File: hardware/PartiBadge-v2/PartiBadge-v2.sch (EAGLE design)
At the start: 29 parts, among them IC2 TSMP58000, J1 I2C, J2 Supply, U1 1042

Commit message: mode switch to power and other cosmetic changes
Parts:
- removed R8: 100, rcl:R-US_M0805
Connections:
- removed net N$2: PHOTON.D2, S5.P
- removed net N$3: R8.1, S5.S
- new net NC: S5.S
- new net ON: IC1.IN, S5.O
- net +3V3: no longer R8.2
- net BATT: now also S5.P; no longer IC1.IN
- net CENT: now also PHOTON.D2; no longer PHOTON.D3
- net DOWN: now also PHOTON.D5; no longer PHOTON.D6
- net GND: no longer S5.O
- net LEFT: now also PHOTON.D4; no longer PHOTON.D5
- net RIGHT: now also PHOTON.D3; no longer PHOTON.D4
- net UP: now also PHOTON.D6; no longer PHOTON.D7
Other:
- moved on the sheet: S5, U1
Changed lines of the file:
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@@
 <?xml version="1.0" encoding="utf-8"?>
 <!DOCTYPE eagle SYSTEM "eagle.dtd">
-<eagle version="9.0.1">
+<eagle version="9.1.0">
 <drawing>
 <settings>
@@
 <part name="JOYSTICK" library="SparkFun-Switches" library_urn="urn:adsk.eagle:library:535" deviceset="JOYSTICK_MINI" device="" package3d_urn="urn:adsk.eagle:package:40157/1"/>
 <part name="GND6" library="supply1" library_urn="urn:adsk.eagle:library:371" deviceset="GND" device=""/>
-<part name="+3V6" library="supply1" library_urn="urn:adsk.eagle:library:371" deviceset="+3V3" device=""/>
 <part name="PARTIFRAME" library="SparkFun-Aesthetics" library_urn="urn:adsk.eagle:library:507" deviceset="FRAME-LETTER" device="NO_PACKAGE" package3d_urn="urn:adsk.eagle:package:37104/1">
 <attribute name="DESIGNER" value="Brandon Satrom"/>
 </part>
-<part name="R8" library="rcl" library_urn="urn:adsk.eagle:library:334" deviceset="R-US_" device="M0805" package3d_urn="urn:adsk.eagle:package:23556/1" value="100"/>
 <part name="PHOTON" library="Particle-Devices" deviceset="PHOTON" device="_WITH_HEADERS"/>
 <part name="U$5" library="tft_1.8_1.44_oled_0.96" deviceset="OLED_0.96_I2C" device=""/>
@@
 <part name="+3V5" library="supply1" library_urn="urn:adsk.eagle:library:371" deviceset="+3V3" device=""/>
 <part name="GND10" library="supply1" library_urn="urn:adsk.eagle:library:371" deviceset="GND" device=""/>
-<part name="GND11" library="supply1" library_urn="urn:adsk.eagle:library:371" deviceset="GND" device=""/>
 <part name="IC1" library="v-reg" library_urn="urn:adsk.eagle:library:409" deviceset="78XXS" device="" package3d_urn="urn:adsk.eagle:package:30342/1"/>
 <part name="GND9" library="supply1" library_urn="urn:adsk.eagle:library:371" deviceset="GND" device=""/>
@@
 <attribute name="VALUE" x="-35.549109375" y="71.114559375" size="1.679990625" layer="96"/>
 </instance>
-<instance part="S5" gate="1" x="68.58" y="40.64"/>
+<instance part="S5" gate="1" x="35.56" y="116.84" rot="MR0"/>
 <instance part="R5" gate="G$1" x="104.14" y="66.04" rot="R90"/>
 <instance part="R6" gate="G$1" x="124.46" y="66.04" rot="R90"/>
@@
 <instance part="JOYSTICK" gate="G$1" x="104.14" y="116.84"/>
 <instance part="GND6" gate="1" x="81.28" y="114.3" rot="R270"/>
-<instance part="+3V6" gate="G$1" x="86.36" y="58.42"/>
 <instance part="PARTIFRAME" gate="G$1" x="-60.96" y="-40.64" smashed="yes">
 <attribute name="DESIGNER" x="-60.96" y="-40.64" size="1.778" layer="96" display="off"/>
@@
 </instance>
 <instance part="PARTIFRAME" gate="V" x="86.36" y="-40.64"/>
-<instance part="R8" gate="G$1" x="86.36" y="48.26" rot="R90"/>
 <instance part="PHOTON" gate="G$1" x="35.56" y="58.42"/>
 <instance part="U$5" gate="G$1" x="-15.24" y="111.76" rot="R270"/>
@@
 <instance part="C2" gate="G$1" x="63.5" y="-20.32"/>
 <instance part="+3V5" gate="G$1" x="81.28" y="-5.08"/>
-<instance part="GND10" gate="1" x="60.96" y="106.68"/>
-<instance part="GND11" gate="1" x="78.74" y="43.18" rot="R90"/>
+<instance part="GND10" gate="1" x="73.66" y="106.68"/>
 <instance part="IC1" gate="1" x="20.32" y="124.46" rot="R180"/>
 <instance part="GND9" gate="1" x="35.56" y="127"/>
@@
 <instance part="VDD2" gate="G$1" x="7.62" y="129.54"/>
 <instance part="IC2" gate="G$1" x="53.34" y="-10.16" rot="R180"/>
-<instance part="U1" gate="G$1" x="55.88" y="116.84" rot="R180"/>
+<instance part="U1" gate="G$1" x="68.58" y="116.84" rot="R180"/>
 </instances>
 <busses>
@@
 </segment>
 <segment>
-<pinref part="S5" gate="1" pin="O"/>
-<pinref part="GND11" gate="1" pin="GND"/>
-<wire x1="76.2" y1="43.18" x2="73.66" y2="43.18" width="0.1524" layer="91"/>
-</segment>
-<segment>
 <pinref part="IC1" gate="1" pin="GND"/>
 <pinref part="GND9" gate="1" pin="GND"/>
@@
 <pinref part="U1" gate="G$1" pin="NEG"/>
 <pinref part="GND10" gate="1" pin="GND"/>
-<wire x1="55.88" y1="116.84" x2="60.96" y2="116.84" width="0.1524" layer="91"/>
-<wire x1="60.96" y1="116.84" x2="60.96" y2="109.22" width="0.1524" layer="91"/>
+<wire x1="68.58" y1="116.84" x2="73.66" y2="116.84" width="0.1524" layer="91"/>
+<wire x1="73.66" y1="116.84" x2="73.66" y2="109.22" width="0.1524" layer="91"/>
 </segment>
 </net>
@@
 <pinref part="+3V4" gate="G$1" pin="+3V3"/>
 <wire x1="127" y1="12.7" x2="127" y2="17.78" width="0.1524" layer="91"/>
-</segment>
-<segment>
-<pinref part="R8" gate="G$1" pin="2"/>
-<pinref part="+3V6" gate="G$1" pin="+3V3"/>
-<wire x1="86.36" y1="53.34" x2="86.36" y2="55.88" width="0.1524" layer="91"/>
 </segment>
 <segment>
@@
 <segment>
 <pinref part="PHOTON" gate="G$1" pin="D0"/>
-<wire x1="53.34" y1="30.48" x2="58.42" y2="30.48" width="0.1524" layer="91"/>
-<label x="53.34" y="30.48" size="1.778" layer="95"/>
+<wire x1="53.34" y1="30.48" x2="66.04" y2="30.48" width="0.1524" layer="91"/>
+<label x="58.42" y="30.48" size="1.778" layer="95"/>
 </segment>
 <segment>
@@
 <segment>
 <pinref part="PHOTON" gate="G$1" pin="D1"/>
-<wire x1="53.34" y1="35.56" x2="58.42" y2="35.56" width="0.1524" layer="91"/>
-<label x="53.34" y="35.56" size="1.778" layer="95"/>
+<wire x1="53.34" y1="35.56" x2="66.04" y2="35.56" width="0.1524" layer="91"/>
+<label x="58.42" y="35.56" size="1.778" layer="95"/>
 </segment>
 <segment>
@@
 </segment>
 <segment>
-<pinref part="PHOTON" gate="G$1" pin="D7"/>
-<wire x1="53.34" y1="66.04" x2="63.5" y2="66.04" width="0.1524" layer="91"/>
-<label x="60.96" y="66.04" size="1.778" layer="95"/>
+<pinref part="PHOTON" gate="G$1" pin="D6"/>
+<wire x1="53.34" y1="60.96" x2="66.04" y2="60.96" width="0.1524" layer="91"/>
+<label x="58.42" y="60.96" size="1.778" layer="95"/>
 </segment>
 </net>
@@
 </segment>
 <segment>
-<pinref part="PHOTON" gate="G$1" pin="D6"/>
-<wire x1="53.34" y1="60.96" x2="63.5" y2="60.96" width="0.1524" layer="91"/>
-<label x="56.642" y="60.96" size="1.778" layer="95"/>
+<pinref part="PHOTON" gate="G$1" pin="D5"/>
+<wire x1="53.34" y1="55.88" x2="66.04" y2="55.88" width="0.1524" layer="91"/>
+<label x="58.42" y="55.88" size="1.778" layer="95"/>
 </segment>
 </net>
@@
 </segment>
 <segment>
-<pinref part="PHOTON" gate="G$1" pin="D5"/>
-<wire x1="53.34" y1="55.88" x2="63.5" y2="55.88" width="0.1524" layer="91"/>
-<label x="58.42" y="55.88" size="1.778" layer="95"/>
+<pinref part="PHOTON" gate="G$1" pin="D4"/>
+<wire x1="53.34" y1="50.8" x2="66.04" y2="50.8" width="0.1524" layer="91"/>
+<label x="58.674" y="51.054" size="1.778" layer="95"/>
 </segment>
 </net>
@@
 </segment>
 <segment>
-<pinref part="PHOTON" gate="G$1" pin="D4"/>
-<wire x1="53.34" y1="50.8" x2="63.5" y2="50.8" width="0.1524" layer="91"/>
-<label x="56.896" y="51.054" size="1.778" layer="95"/>
+<pinref part="PHOTON" gate="G$1" pin="D3"/>
+<wire x1="53.34" y1="45.72" x2="66.04" y2="45.72" width="0.1524" layer="91"/>
+<label x="58.42" y="45.72" size="1.778" layer="95"/>
 </segment>
 </net>
@@
 </segment>
 <segment>
-<pinref part="PHOTON" gate="G$1" pin="D3"/>
-<wire x1="53.34" y1="45.72" x2="63.5" y2="45.72" width="0.1524" layer="91"/>
-<label x="58.42" y="45.72" size="1.778" layer="95"/>
+<pinref part="PHOTON" gate="G$1" pin="D2"/>
+<wire x1="53.34" y1="40.64" x2="66.04" y2="40.64" width="0.1524" layer="91"/>
+<label x="58.42" y="40.64" size="1.778" layer="95"/>
 </segment>
 </net>
@@
 </segment>
 </net>
-<net name="N$2" class="0">
-<segment>
-<pinref part="PHOTON" gate="G$1" pin="D2"/>
-<pinref part="S5" gate="1" pin="P"/>
-<wire x1="53.34" y1="40.64" x2="66.04" y2="40.64" width="0.1524" layer="91"/>
-</segment>
-</net>
-<net name="N$3" class="0">
-<segment>
-<pinref part="S5" gate="1" pin="S"/>
-<wire x1="73.66" y1="38.1" x2="86.36" y2="38.1" width="0.1524" layer="91"/>
-<pinref part="R8" gate="G$1" pin="1"/>
-<wire x1="86.36" y1="38.1" x2="86.36" y2="43.18" width="0.1524" layer="91"/>
-</segment>
-</net>
 <net name="5V" class="0">
 <segment>
@@
 <net name="BATT" class="0">
 <segment>
+<pinref part="U1" gate="G$1" pin="POS"/>
+<pinref part="S5" gate="1" pin="P"/>
+<wire x1="43.18" y1="116.84" x2="38.1" y2="116.84" width="0.1524" layer="91"/>
+</segment>
+</net>
+<net name="ON" class="0">
+<segment>
+<pinref part="S5" gate="1" pin="O"/>
 <pinref part="IC1" gate="1" pin="IN"/>
-<pinref part="U1" gate="G$1" pin="POS"/>
-<wire x1="27.94" y1="124.46" x2="30.48" y2="124.46" width="0.1524" layer="91"/>
-<wire x1="30.48" y1="124.46" x2="30.48" y2="116.84" width="0.1524" layer="91"/>
-</segment>
-</net>
+<wire x1="30.48" y1="119.38" x2="30.48" y2="124.46" width="0.1524" layer="91"/>
+<wire x1="30.48" y1="124.46" x2="27.94" y2="124.46" width="0.1524" layer="91"/>
+<label x="30.48" y="119.38" size="1.778" layer="95" rot="R90"/>
+</segment>
+</net>
+<net name="NC" class="0">
+<segment>
+<pinref part="S5" gate="1" pin="S"/>
+<wire x1="30.48" y1="114.3" x2="25.4" y2="114.3" width="0.1524" layer="91"/>
+<label x="25.4" y="114.3" size="1.778" layer="95"/>
+</segment>
+</net>

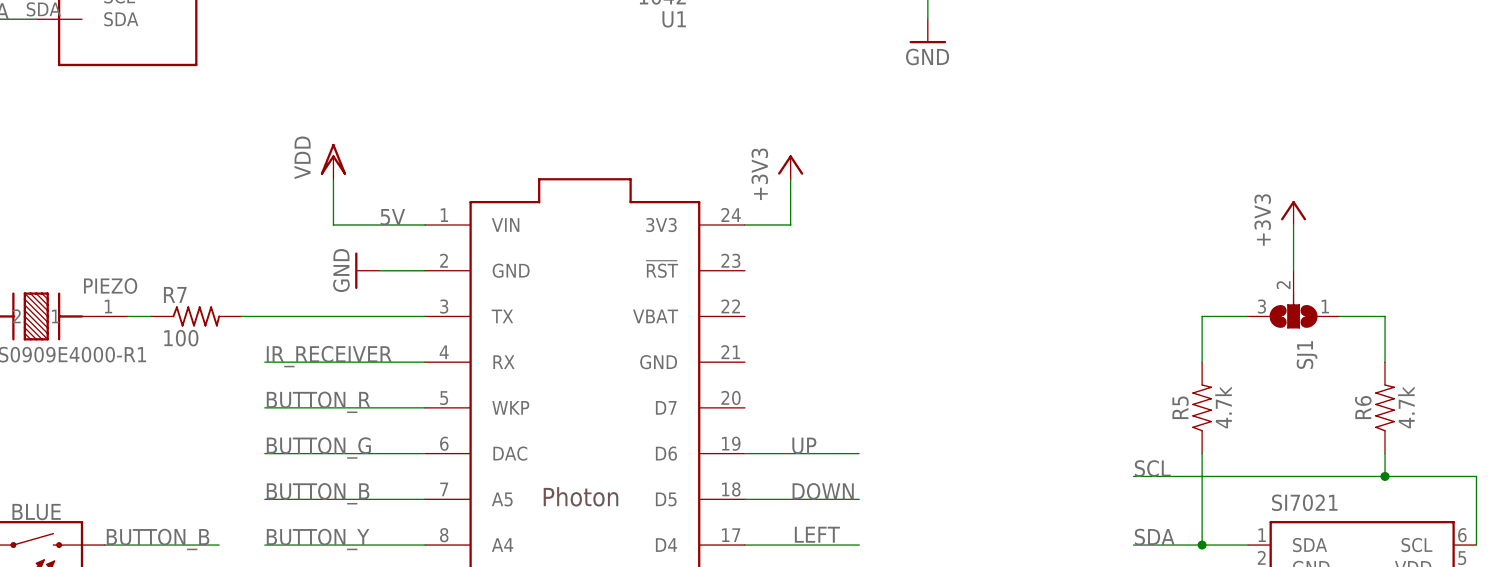
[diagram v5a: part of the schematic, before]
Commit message: updated schematic and layout based on feedback from Brett
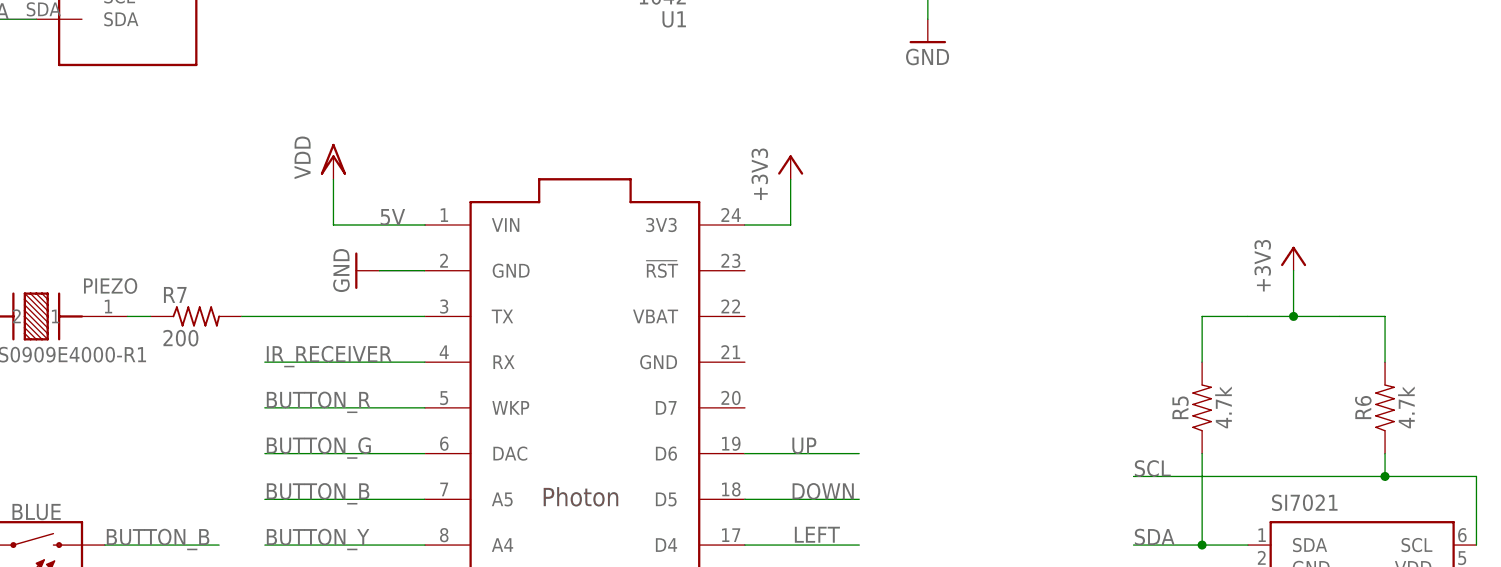
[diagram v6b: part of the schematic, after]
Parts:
- removed SJ1: (no value), jumper:SJ2W
- R7: value 100 -> 200
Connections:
- removed net N$11: R5.2, SJ1.3
- removed net N$12: R6.2, SJ1.1
- net +3V3: now also R5.2, R6.2; no longer SJ1.2
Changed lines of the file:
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@@
 <part name="R6" library="SparkFun-Resistors" library_urn="urn:adsk.eagle:library:532" deviceset="4.7KOHM" device="-0603-1/10W-1%" package3d_urn="urn:adsk.eagle:package:39650/1" value="4.7k"/>
 <part name="C1" library="SparkFun-Capacitors" library_urn="urn:adsk.eagle:library:510" deviceset="0.1UF" device="-0603-25V-(+80/-20%)" package3d_urn="urn:adsk.eagle:package:37414/1" value="0.1uF"/>
-<part name="SJ1" library="jumper" library_urn="urn:adsk.eagle:library:252" deviceset="SJ2W" device="" package3d_urn="urn:adsk.eagle:package:15474/1"/>
 <part name="GND1" library="supply1" library_urn="urn:adsk.eagle:library:371" deviceset="GND" device=""/>
 <part name="GND2" library="supply1" library_urn="urn:adsk.eagle:library:371" deviceset="GND" device=""/>
@@
 <part name="J1" library="SparkFun-Connectors" library_urn="urn:adsk.eagle:library:513" deviceset="CONN_02" device="" package3d_urn="urn:adsk.eagle:package:38039/1" value="I2C"/>
 <part name="J2" library="SparkFun-Connectors" library_urn="urn:adsk.eagle:library:513" deviceset="CONN_02" device="" package3d_urn="urn:adsk.eagle:package:38039/1" value="Supply"/>
-<part name="R7" library="rcl" library_urn="urn:adsk.eagle:library:334" deviceset="R-US_" device="M0805" package3d_urn="urn:adsk.eagle:package:23556/1" value="100"/>
+<part name="R7" library="rcl" library_urn="urn:adsk.eagle:library:334" deviceset="R-US_" device="M0805" package3d_urn="urn:adsk.eagle:package:23556/1" value="200"/>
 <part name="JOYSTICK" library="SparkFun-Switches" library_urn="urn:adsk.eagle:library:535" deviceset="JOYSTICK_MINI" device="" package3d_urn="urn:adsk.eagle:package:40157/1"/>
 <part name="GND6" library="supply1" library_urn="urn:adsk.eagle:library:371" deviceset="GND" device=""/>
@@
 <instance part="R6" gate="G$1" x="124.46" y="66.04" rot="R90"/>
 <instance part="C1" gate="G$1" x="147.32" y="40.64"/>
-<instance part="SJ1" gate="G$1" x="114.3" y="76.2" rot="R270"/>
 <instance part="GND1" gate="1" x="147.32" y="33.02"/>
 <instance part="GND2" gate="1" x="104.14" y="45.72"/>
-<instance part="+3V1" gate="G$1" x="114.3" y="88.9"/>
+<instance part="+3V1" gate="G$1" x="114.3" y="83.82"/>
 <instance part="+3V2" gate="G$1" x="147.32" y="58.42"/>
 <instance part="GND3" gate="1" x="-35.56" y="66.04"/>
@@
 <segment>
 <pinref part="+3V1" gate="G$1" pin="+3V3"/>
-<pinref part="SJ1" gate="G$1" pin="2"/>
-<wire x1="114.3" y1="86.36" x2="114.3" y2="81.28" width="0.1524" layer="91"/>
+<wire x1="114.3" y1="81.28" x2="114.3" y2="76.2" width="0.1524" layer="91"/>
+<pinref part="R5" gate="G$1" pin="2"/>
+<wire x1="104.14" y1="71.12" x2="104.14" y2="76.2" width="0.1524" layer="91"/>
+<wire x1="104.14" y1="76.2" x2="109.22" y2="76.2" width="0.1524" layer="91"/>
+<wire x1="109.22" y1="76.2" x2="114.3" y2="76.2" width="0.1524" layer="91"/>
+<pinref part="R6" gate="G$1" pin="2"/>
+<wire x1="119.38" y1="76.2" x2="124.46" y2="76.2" width="0.1524" layer="91"/>
+<wire x1="124.46" y1="76.2" x2="124.46" y2="71.12" width="0.1524" layer="91"/>
+<wire x1="119.38" y1="76.2" x2="114.3" y2="76.2" width="0.1524" layer="91"/>
+<junction x="114.3" y="76.2"/>
 </segment>
 <segment>
@@
 </segment>
 </net>
-<net name="N$11" class="0">
-<segment>
-<pinref part="R5" gate="G$1" pin="2"/>
-<pinref part="SJ1" gate="G$1" pin="3"/>
-<wire x1="104.14" y1="71.12" x2="104.14" y2="76.2" width="0.1524" layer="91"/>
-<wire x1="104.14" y1="76.2" x2="109.22" y2="76.2" width="0.1524" layer="91"/>
-</segment>
-</net>
-<net name="N$12" class="0">
-<segment>
-<pinref part="SJ1" gate="G$1" pin="1"/>
-<pinref part="R6" gate="G$1" pin="2"/>
-<wire x1="119.38" y1="76.2" x2="124.46" y2="76.2" width="0.1524" layer="91"/>
-<wire x1="124.46" y1="76.2" x2="124.46" y2="71.12" width="0.1524" layer="91"/>
-</segment>
-</net>

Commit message: additional layout tweaks
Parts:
- added D7: (no value), SparkFun-Connectors:CONN_01
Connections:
- new net D7: D7.1, PHOTON.D7
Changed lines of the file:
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@@
 <part name="IC2" library="TSMP58000" deviceset="TSMP58000" device=""/>
 <part name="U1" library="1042" deviceset="1042" device=""/>
+<part name="D7" library="SparkFun-Connectors" library_urn="urn:adsk.eagle:library:513" deviceset="CONN_01" device="" package3d_urn="urn:adsk.eagle:package:38028/1"/>
 </parts>
 <sheets>
@@
 <instance part="IC2" gate="G$1" x="53.34" y="-10.16" rot="R180"/>
 <instance part="U1" gate="G$1" x="68.58" y="116.84" rot="R180"/>
+<instance part="D7" gate="G$1" x="78.74" y="66.04" rot="R180"/>
 </instances>
 <busses>
@@
 </segment>
 </net>
+<net name="D7" class="0">
+<segment>
+<pinref part="D7" gate="G$1" pin="1"/>
+<pinref part="PHOTON" gate="G$1" pin="D7"/>
+<wire x1="71.12" y1="66.04" x2="53.34" y2="66.04" width="0.1524" layer="91"/>
+</segment>
+</net>

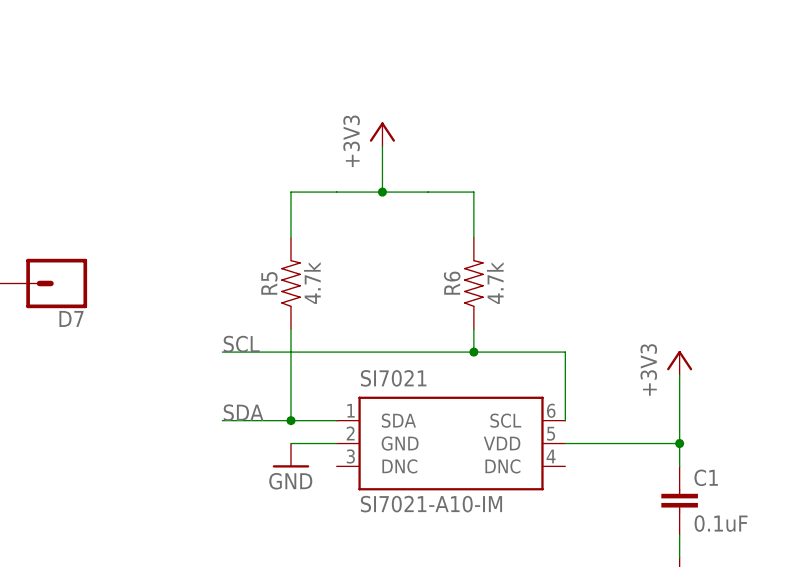
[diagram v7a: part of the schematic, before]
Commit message: fix D7 breakout placement
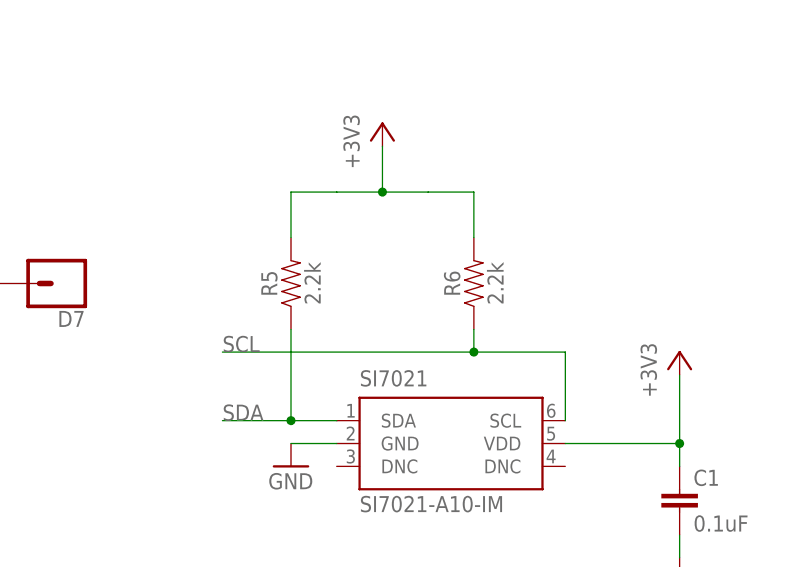
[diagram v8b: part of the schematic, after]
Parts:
- R5, R6: value 4.7k -> 2.2k
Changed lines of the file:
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@@
 <part name="PIEZO" library="PKMCS0909E4000-R1" deviceset="PKMCS0909E4000-R1" device=""/>
 <part name="S5" library="SparkFun-Switches" library_urn="urn:adsk.eagle:library:535" deviceset="SWITCH-SPDT" device="-PTH-11.6X4.0MM" package3d_urn="urn:adsk.eagle:package:40177/1"/>
-<part name="R5" library="SparkFun-Resistors" library_urn="urn:adsk.eagle:library:532" deviceset="4.7KOHM" device="-0603-1/10W-1%" package3d_urn="urn:adsk.eagle:package:39650/1" value="4.7k"/>
-<part name="R6" library="SparkFun-Resistors" library_urn="urn:adsk.eagle:library:532" deviceset="4.7KOHM" device="-0603-1/10W-1%" package3d_urn="urn:adsk.eagle:package:39650/1" value="4.7k"/>
+<part name="R5" library="SparkFun-Resistors" library_urn="urn:adsk.eagle:library:532" deviceset="4.7KOHM" device="-0603-1/10W-1%" package3d_urn="urn:adsk.eagle:package:39650/1" value="2.2k"/>
+<part name="R6" library="SparkFun-Resistors" library_urn="urn:adsk.eagle:library:532" deviceset="4.7KOHM" device="-0603-1/10W-1%" package3d_urn="urn:adsk.eagle:package:39650/1" value="2.2k"/>
 <part name="C1" library="SparkFun-Capacitors" library_urn="urn:adsk.eagle:library:510" deviceset="0.1UF" device="-0603-25V-(+80/-20%)" package3d_urn="urn:adsk.eagle:package:37414/1" value="0.1uF"/>
 <part name="GND1" library="supply1" library_urn="urn:adsk.eagle:library:371" deviceset="GND" device=""/>
